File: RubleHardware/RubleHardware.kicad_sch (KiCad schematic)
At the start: 28 parts, among them IC1 LTC3780EUH#PBF, Q1 NMOS_Substrate, Q2 NMOS_Substrate, Q3 NMOS_Substrate, Q4 NMOS_Substrate

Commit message: feat: Adding in values to board
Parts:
- removed C2, C3: C_Small, symbol Device:C_Small
- removed R5, R6: R_Small, symbol Device:R_Small
- added PGOOD: LED, symbol Device:LED
- added R1_12v: 8.06k, symbol Device:R_Small
- added R1_3: 66.5, symbol Device:R_Small
- added Rpu: 200, symbol Device:R_Small
- added Rpu1: 220, symbol Device:R_Small
- added Rpu2: 390, symbol Device:R_Small
- CSENS: renamed from C1; value C_Small -> 68p
- Ca: renamed from C7; value C_Small -> 0.22u
- Cb: renamed from C8; value C_Small -> 0.22u
- Cf: renamed from C5; value C_Small -> 0.1u
- Cin: renamed from C10; value C_Small -> 22u
- Cout: renamed from C9; value C_Small -> 330u
- Css: renamed from C4; value C_Small -> 0.022u
- Cvcc: renamed from C6; value C_Small -> 4.7u
- L: renamed from L1; value L_Small -> 6.8u
- R1_2: renamed from R3; value R_Small -> 11.5
- R2: renamed from R4; value R_Small -> 113k
- RSENS+: renamed from R1; value R_Small -> 100
- RSENS-: renamed from R2; value R_Small -> 100
- Rin: renamed from R8; value R_Small -> 10
- Rsense: renamed from R7; value R_Small -> 10m
- renumbered Q1 to A, Q3 to B, Q2 to C, Q4 to D, D4 to D1, D3 to D2, D2 to Da, D1 to Db
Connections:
- net GND: now also Cin.1, Cout.2, Css.1, IC1.33 (SGND_2), IC1.7 (FCB), IC1.8 (PLLFTR), R1_2.1, PGOOD.1 (K), R1_3.1, Rpu.1
- net ICVOUT: now also R2.1; no longer R2.2
- net at IC1.30 (PGOOD): now also Rpu1.2
- removed net GNDS: Cin.1, Cout.2, Css.1, IC1.10 (PLLIN), IC1.11 (STBYMD), IC1.33 (SGND_2), IC1.5 (SGND_1), IC1.7 (FCB), R1_2.2
- new net: Rpu.2, Rpu1.1, Rpu2.1
- new net: PGOOD.2 (A), Rpu2.2
- new net: IC1.4 (VOSENSE), R1_12v.2, R1_2.2, R2.2
- new net: R1_2.1, R1_3.2
- new net: R1_12v.1, R1_2.2
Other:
- note added: "24V"
- note added: "36V"
- moved on the sheet: A, B, C, CSENS, Ca, Cb, Cf, Cin, Cout, Css, Cvcc, D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

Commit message: feat: First review feedback
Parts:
- removed R1_3: 66.5, symbol Device:R_Small
- removed Rpu: 200, symbol Device:R_Small
- removed Rpu1: 220, symbol Device:R_Small
- added C1: 10nF, symbol Device:C_Small
- added C2: 47pF, symbol Device:C_Small
- added D3: LED, symbol Device:LED
- added H1, H2, H3, H4: MountingHole_Pad, MountingHole:MountingHole_3.2mm_M3_DIN965_Pad, symbol Mechanical:MountingHole_Pad
- added J1_IN, J2_OUT: Conn_01x08_Male, iclr:Molex_Mini-Fit_Jr_5569-08A2_2x04_P4.20mm_Horizontal, symbol Connector:Conn_01x08_Male
- added JP1: SolderJumper_3_Open, symbol Jumper:SolderJumper_3_Open
- added R1: 1k, symbol Device:R_Small
- added R4: 100k, symbol Device:R_Small
- added TP1, TP2: TestPoint, symbol Connector:TestPoint
- A, B, C, D: value NMOS_Substrate -> BUK9M11-40E
- CSENS: value 68p -> 68pF
- Ca: value 0.22u -> 0.22uF
- Cin: value 22u -> 22uF
- Cout: value 330u -> 330uF
- Css: value 0.022u -> 22nF
- D1, D2: value D_Schottky_Small -> DST1550S
- Da, Db: value D_Schottky_Small -> B0540W-7-F
- L: value 6.8u -> 6.8uH
- R1_24v: renamed from R1_2; value 11.5 -> 3.89k
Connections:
- net GND: now also IC1.10 (PLLIN), IC1.11 (STBYMD), IC1.5 (SGND_1), R1_12v.1, C1.1, C2.1, H1.1, H2.1, H3.1, H4.1, J1_IN.1 (Pin_1), J1_IN.2 (Pin_2), J1_IN.3 (Pin_3), J2_OUT.1 (Pin_1), J2_OUT.2 (Pin_2), J2_OUT.3 (Pin_3), R1.2; no longer PGOOD.1 (K)
- net ICVIN: now also J1_IN.5 (Pin_5), J1_IN.6 (Pin_6), TP2.1
- net ICVOUT: now also D3.2 (A), J2_OUT.5 (Pin_5), J2_OUT.6 (Pin_6), TP1.1
- net INTVCC: now also PGOOD.2 (A)
- net at Rpu2.1: now also IC1.30 (PGOOD)
- net at Rpu2.2: now also PGOOD.1 (K); no longer PGOOD.2 (A)
- net at IC1.4 (VOSENSE), R2.2: now also JP1.2 (C); no longer R1_12v.2, R1_24v.2
- net at IC1.3 (ITH): now also C2.2, R4.2
- net at R1_24v.2: now also JP1.3 (B); no longer R1_12v.1
- new net: D3.1 (K), R1.1
- new net: C1.2, R4.1
- new net: JP1.1 (A), R1_12v.2
- new net +3V3: J1_IN.4 (Pin_4), J2_OUT.4 (Pin_4)
- new net CAN+: J1_IN.8 (Pin_8), J2_OUT.8 (Pin_8)
- new net CAN-: J1_IN.7 (Pin_7), J2_OUT.7 (Pin_7)
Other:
- moved on the sheet: A, B, C, CSENS, Ca, Cb, Cf, Cin, Cout, Css, Cvcc, D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

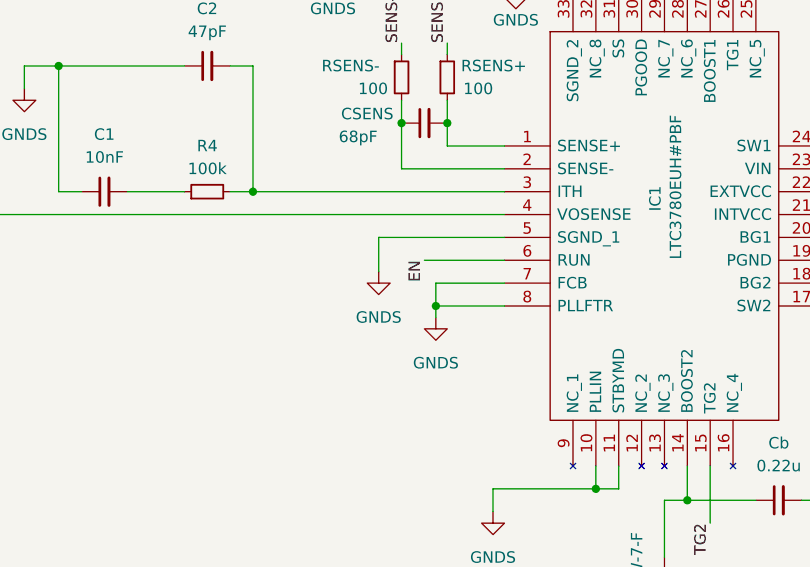
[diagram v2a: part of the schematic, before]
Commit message: feat: Pulled up enable pin
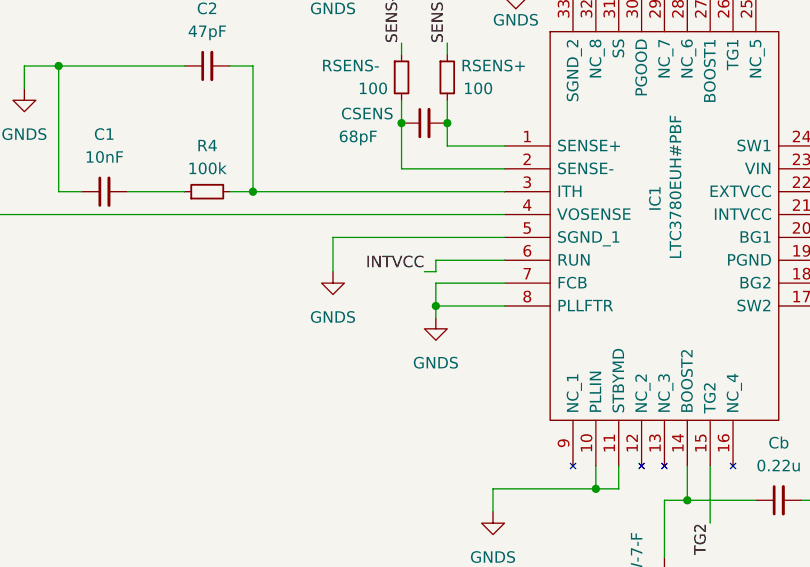
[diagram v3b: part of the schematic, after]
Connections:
- net EN is gone; now on net INTVCC: IC1.6 (RUN)
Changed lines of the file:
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@@
 	(wire
 		(pts
+			(xy 110.49 133.35) (xy 118.11 133.35)
+		)
+		(stroke
+			(width 0)
+			(type default)
+		)
+	)
+	(wire
+		(pts
 			(xy 153.67 135.89) (xy 156.21 135.89)
 		)
@@
 	(wire
 		(pts
+			(xy 110.49 134.62) (xy 110.49 133.35)
+		)
+		(stroke
+			(width 0)
+			(type default)
+		)
+	)
+	(wire
+		(pts
 			(xy 215.9 125.73) (xy 218.44 125.73)
 		)
@@
 	(wire
 		(pts
-			(xy 118.11 133.35) (xy 109.22 133.35)
+			(xy 110.49 134.62) (xy 109.22 134.62)
 		)
 		(stroke
@@
 	(wire
 		(pts
-			(xy 104.14 130.81) (xy 118.11 130.81)
+			(xy 99.06 130.81) (xy 118.11 130.81)
 		)
 		(stroke
@@
 	(wire
 		(pts
-			(xy 104.14 130.81) (xy 104.14 134.62)
+			(xy 99.06 130.81) (xy 99.06 134.62)
 		)
 		(stroke
@@
 		)
 	)
-	(label "EN"
-		(at 109.22 133.35 270)
+	(label "INTVCC"
+		(at 109.22 134.62 180)
 		(effects
 			(font
@@
 	(symbol
 		(lib_id "power:GNDS")
-		(at 104.14 134.62 0)
+		(at 99.06 134.62 0)
 		(unit 1)
 		(exclude_from_sim no)
@@
 		(fields_autoplaced yes)
 		(property "Reference" "#PWR08"
-			(at 104.14 140.97 0)
+			(at 99.06 140.97 0)
 			(effects
 				(font
@@
 		)
 		(property "Value" "GNDS"
-			(at 104.14 139.7 0)
+			(at 99.06 139.7 0)
 			(effects
 				(font
@@
 		)
 		(property "Footprint" ""
-			(at 104.14 134.62 0)
+			(at 99.06 134.62 0)
 			(effects
 				(font
@@
 		)
 		(property "Datasheet" ""
-			(at 104.14 134.62 0)
+			(at 99.06 134.62 0)
 			(effects
 				(font
@@
 		)
 		(property "Description" "Power symbol creates a global label with name \"GNDS\" , signal ground"
-			(at 104.14 134.62 0)
+			(at 99.06 134.62 0)
 			(effects
 				(font

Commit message: feat: Changes almost complete for feedbak
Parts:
- L: value 6.8uH -> 18uH
- Rsense: value 10m -> 1.9m
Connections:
- net GND: no longer IC1.8 (PLLFTR), J1_IN.3 (Pin_3), J2_OUT.3 (Pin_3)
- new net GND1: J1_IN.3 (Pin_3), J2_OUT.3 (Pin_3)
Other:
- moved on the sheet: R1_12v, R1_24v

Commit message: feat: Update vout and vin caps
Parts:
- removed Cin: 22uF, symbol Device:C_Small
- added Cin1: 100nF, symbol Device:C_Small
- added Cin2: 2uF, symbol Device:C_Small
- Cout2: renamed from Cout; value 330uF -> 2uF
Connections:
- net GND: now also Cin1.1, Cin2.1
- net ICVIN: now also Cin1.2, Cin2.2
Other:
- moved on the sheet: Cout3

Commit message: feat: Stopped being stupid and connected grounds
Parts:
- added Cout1: 330uF, symbol Device:C_Small
- added Cout2: 2uF, symbol Device:C_Small
- Cout3: renamed from Cout2; value 2uF -> 100nF
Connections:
- net GND1 is gone; now on net GND: J1_IN.3 (Pin_3), J2_OUT.3 (Pin_3)
- net GND: now also Cout1.2, Cout2.2
- net ICVOUT: now also Cout1.1, Cout2.1
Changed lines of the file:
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@@
 	)
 	(junction
+		(at 149.86 35.56)
+		(diameter 0)
+		(color 0 0 0 0)
+	)
+	(junction
 		(at 257.81 104.14)
 		(diameter 0)
@@
 	)
 	(junction
+		(at 100.33 35.56)
+		(diameter 0)
+		(color 0 0 0 0)
+	)
+	(junction
 		(at 158.75 123.19)
 		(diameter 0)
@@
 	(wire
 		(pts
-			(xy 152.4 25.4) (xy 152.4 35.56)
-		)
-		(stroke
-			(width 0)
-			(type default)
-		)
-	)
-	(wire
-		(pts
 			(xy 143.51 96.52) (xy 143.51 102.87)
 		)
@@
 	(wire
 		(pts
-			(xy 99.06 25.4) (xy 102.87 25.4)
-		)
-		(stroke
-			(width 0)
-			(type default)
-		)
-	)
-	(wire
-		(pts
 			(xy 139.7 73.66) (xy 139.7 76.2)
 		)
@@
 	(wire
 		(pts
-			(xy 148.59 27.94) (xy 148.59 25.4)
-		)
-		(stroke
-			(width 0)
-			(type default)
-		)
-	)
-	(wire
-		(pts
 			(xy 139.7 76.2) (xy 146.05 76.2)
 		)
@@
 	(wire
 		(pts
+			(xy 149.86 35.56) (xy 152.4 35.56)
+		)
+		(stroke
+			(width 0)
+			(type default)
+		)
+	)
+	(wire
+		(pts
 			(xy 257.81 116.84) (xy 257.81 120.65)
 		)
@@
 	(wire
 		(pts
-			(xy 148.59 25.4) (xy 152.4 25.4)
-		)
-		(stroke
-			(width 0)
-			(type default)
-		)
-	)
-	(wire
-		(pts
 			(xy 198.12 106.68) (xy 198.12 125.73)
 		)
@@
 	(wire
 		(pts
+			(xy 100.33 35.56) (xy 102.87 35.56)
+		)
+		(stroke
+			(width 0)
+			(type default)
+		)
+	)
+	(wire
+		(pts
 			(xy 257.81 127) (xy 264.16 127)
 		)
@@
 	(wire
 		(pts
-			(xy 99.06 27.94) (xy 99.06 25.4)
-		)
-		(stroke
-			(width 0)
-			(type default)
-		)
-	)
-	(wire
-		(pts
 			(xy 257.81 104.14) (xy 261.62 104.14)
 		)
@@
 	(wire
 		(pts
-			(xy 102.87 25.4) (xy 102.87 35.56)
-		)
-		(stroke
-			(width 0)
-			(type default)
-		)
-	)
-	(wire
-		(pts
 			(xy 189.23 133.35) (xy 190.5 133.35)
 		)
@@
 	)
 	(symbol
-		(lib_id "power:GND1")
-		(at 99.06 27.94 0)
-		(unit 1)
-		(exclude_from_sim no)
-		(in_bom yes)
-		(on_board yes)
-		(dnp no)
-		(fields_autoplaced yes)
-		(property "Reference" "#PWR013"
-			(at 99.06 34.29 0)
-			(effects
-				(font
-					(size 1.27 1.27)
-				)
-				(hide yes)
-			)
-		)
-		(property "Value" "GND1"
-			(at 99.06 33.02 0)
-			(effects
-				(font
-					(size 1.27 1.27)
-				)
-			)
-		)
-		(property "Footprint" ""
-			(at 99.06 27.94 0)
-			(effects
-				(font
-					(size 1.27 1.27)
-				)
-				(hide yes)
-			)
-		)
-		(property "Datasheet" ""
-			(at 99.06 27.94 0)
-			(effects
-				(font
-					(size 1.27 1.27)
-				)
-				(hide yes)
-			)
-		)
-		(property "Description" "Power symbol creates a global label with name \"GND1\" , ground"
-			(at 99.06 27.94 0)
-			(effects
-				(font
-					(size 1.27 1.27)
-				)
-				(hide yes)
-			)
-		)
-		(pin "1"
-		)
-		(instances
-			(project "RubleHardware"
-				(path "/1d79c16d-d8ab-4199-bd03-3b802e23f067"
-					(reference "#PWR013")
-					(unit 1)
-				)
-			)
-		)
-	)
-	(symbol
 		(lib_id "Mechanical:MountingHole_Pad")
 		(at 259.08 33.02 0)
@@
 					(unit 1)
 				)
-			)
-		)
-	)
-	(symbol
-		(lib_id "power:GND1")
-		(at 148.59 27.94 0)
-		(unit 1)
-		(exclude_from_sim no)
-		(in_bom yes)
-		(on_board yes)
-		(dnp no)
-		(fields_autoplaced yes)
-		(property "Reference" "#PWR010"
-			(at 148.59 34.29 0)
-			(effects
-				(font
-					(size 1.27 1.27)
-				)
-				(hide yes)
-			)
-		)
-		(property "Value" "GND1"
-			(at 148.59 33.02 0)
-			(effects
-				(font
-					(size 1.27 1.27)
-				)
-			)
-		)
-		(property "Footprint" ""
-			(at 148.59 27.94 0)
-			(effects
-				(font
-					(size 1.27 1.27)
-				)
-				(hide yes)
-			)
-		)
-		(property "Datasheet" ""
-			(at 148.59 27.94 0)
-			(effects
-				(font
-					(size 1.27 1.27)
-				)
-				(hide yes)
-			)
-		)
-		(property "Description" "Power symbol creates a global label with name \"GND1\" , ground"
-			(at 148.59 27.94 0)
-			(effects
-				(font
-					(size 1.27 1.27)
-				)
-				(hide yes)
-			)
-		)
-		(pin "1"
-		)
-		(instances
-			(project ""
-				(path "/1d79c16d-d8ab-4199-bd03-3b802e23f067"
-					(reference "#PWR010")
-					(unit 1)
-				)

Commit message: mega commit ;)
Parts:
- removed A, B, C, D: BUK9M11-40E, symbol Simulation_SPICE:NMOS_Substrate
- removed Cout1: 330uF, symbol Device:C_Small
- removed Cout2: 2uF, symbol Device:C_Small
- removed D1, D2: DST1550S, symbol Device:D_Schottky_Small
- added A1, B1, C3, D3: BSZ025N04LS, iclr:BSZ025N04LS, symbol iclr:BSZ025N04LS
- added Cin1: 100uF, Capacitor_Tantalum_SMD:CP_EIA-7360-38_Kemet-E, symbol Device:C_Polarized_Small
- added Cin4: 22uF, iclr:CAPC6050X550N, symbol Device:C_Small
- added Cout2: 330uF, iclr:CAPAE1030X1050N, symbol Device:C_Polarized_Small
- added Cout3: 2.2uF, iclr:RESC2013X65N, symbol Device:C_Small
- added D2, D4: DST1550S, Package_TO_SOT_SMD:TO-277B, symbol Device:D_Schottky_AAK
- C1, C2: footprint (none) -> Capacitor_SMD:C_0402_1005Metric
- CSENS1: renamed from CSENS; footprint (none) -> Capacitor_SMD:C_0402_1005Metric; MFR (none) -> 0603CG680J500NT
- Ca1: renamed from Ca; footprint (none) -> Capacitor_SMD:C_0402_1005Metric
- Cb1: renamed from Cb; footprint (none) -> Capacitor_SMD:C_0402_1005Metric
- Cf1: renamed from Cf; value 0.1u -> 0.1uF; footprint (none) -> Capacitor_SMD:C_0402_1005Metric
- Cin2: renamed from Cin1; value 100nF -> 22uF; footprint (none) -> iclr:CAPC6050X550N; MFR (none) -> CKG57NX5R1H226M500JH
- Cin3: renamed from Cin2; value 2uF -> 22uF; footprint (none) -> iclr:CAPC6050X550N; MFR (none) -> CKG57NX5R1H226M500JH
- Cout1: renamed from Cout3; footprint (none) -> Capacitor_SMD:C_0402_1005Metric
- Css1: renamed from Css; footprint (none) -> Capacitor_SMD:C_0402_1005Metric
- Cvcc1: renamed from Cvcc; value 4.7u -> 4.7uf; footprint (none) -> Capacitor_SMD:C_0402_1005Metric
- D1: renamed from D3; value LED -> LED_GREEN; footprint (none) -> LED_SMD:LED_0402_1005Metric
- Da1: renamed from Da; footprint (none) -> iclr:SODFL3516X70N
- Db1: renamed from Db; footprint (none) -> iclr:SODFL3516X70N
- IC1: footprint QFN50P500X500X80-33N-D -> RubleHardware:QFN-32_UH
- JP1: footprint (none) -> Jumper:SolderJumper-3_P2.0mm_Open_TrianglePad1.0x1.5mm
- L1: renamed from L; footprint (none) -> Inductor_SMD:L_Sunlord_SWPA8040S
- PBAD1: renamed from PGOOD; value LED -> RED_LED; footprint (none) -> LED_SMD:LED_0402_1005Metric
- R1: renamed from R2; footprint (none) -> Resistor_SMD:R_0402_1005Metric_Pad0.72x0.64mm_HandSolder
- R1_12v1: renamed from R1_12v; footprint (none) -> Resistor_SMD:R_0402_1005Metric_Pad0.72x0.64mm_HandSolder
- R1_24v1: renamed from R1_24v; footprint (none) -> iclr:RESC2013X65N; MFR (none) -> 0805W8F3901T5E
- R2: renamed from R4; footprint (none) -> Resistor_SMD:R_0402_1005Metric_Pad0.72x0.64mm_HandSolder
- R3: renamed from R1; value 1k -> 3k; footprint (none) -> Resistor_SMD:R_0402_1005Metric
- RSENS+1: renamed from RSENS+; footprint (none) -> Resistor_SMD:R_0402_1005Metric_Pad0.72x0.64mm_HandSolder
- RSENS-1: renamed from RSENS-; footprint (none) -> Resistor_SMD:R_0402_1005Metric_Pad0.72x0.64mm_HandSolder
- Rin1: renamed from Rin; footprint (none) -> Resistor_SMD:R_0402_1005Metric_Pad0.72x0.64mm_HandSolder
- Rpu1: renamed from Rpu2; footprint (none) -> Resistor_SMD:R_0402_1005Metric_Pad0.72x0.64mm_HandSolder
- Rsense1: renamed from Rsense; footprint (none) -> Resistor_SMD:R_0402_1005Metric_Pad0.72x0.64mm_HandSolder
- TP1, TP2: footprint (none) -> TestPoint:TestPoint_Pad_D1.5mm
- renumbered J1_IN to J1_IN1, J2_OUT to J2_OUT1
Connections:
- net BG1: now also C3.4 (G)
- net BG2: now also B1.4 (G)
- net GND: now also Cin1.2, Cin4.1, Cout2.2, Cout3.2
- net ICVIN: now also A1.5 (D), A1.6 (D), A1.7 (D), A1.8 (D), A1.A5 (D), Cin1.1, Cin4.2
- net ICVOUT: now also Cout2.1, Cout3.1, D3.5 (D), D3.6 (D), D3.7 (D), D3.8 (D), D3.A5 (D), D4.3 (K)
- net SENS-: now also B1.1 (S), B1.2 (S), B1.3 (S), B1.A1 (S), C3.1 (S), C3.2 (S), C3.3 (S), C3.A1 (S), D2.1 (A), D2.2 (A)
- net SW1: now also C3.5 (D), C3.6 (D), C3.7 (D), C3.8 (D), C3.A5 (D), D3.1 (S), D3.2 (S), D3.3 (S), D3.A1 (S), D4.1 (A), D4.2 (A)
- net SW2: now also A1.1 (S), A1.2 (S), A1.3 (S), A1.A1 (S), B1.5 (D), B1.6 (D), B1.7 (D), B1.8 (D), B1.A5 (D), D2.3 (K)
- net TG1: now also D3.4 (G)
- net TG2: now also A1.4 (G)
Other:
- note added: "SWPA8040S180MT"
- moved on the sheet: Cout1
